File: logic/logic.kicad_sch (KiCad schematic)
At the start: 27 parts, among them J1 DIN41612_03x32_ABC, J2 Conn_02x05_Odd_Even, U1 TPIC6595, U2 TPIC6595, U3 TPIC6595, U4 TPIC6595, U5 TPIC6595, U6 TPIC6595, U7 TPIC6595, U8 TPIC6595, U9 74HC14

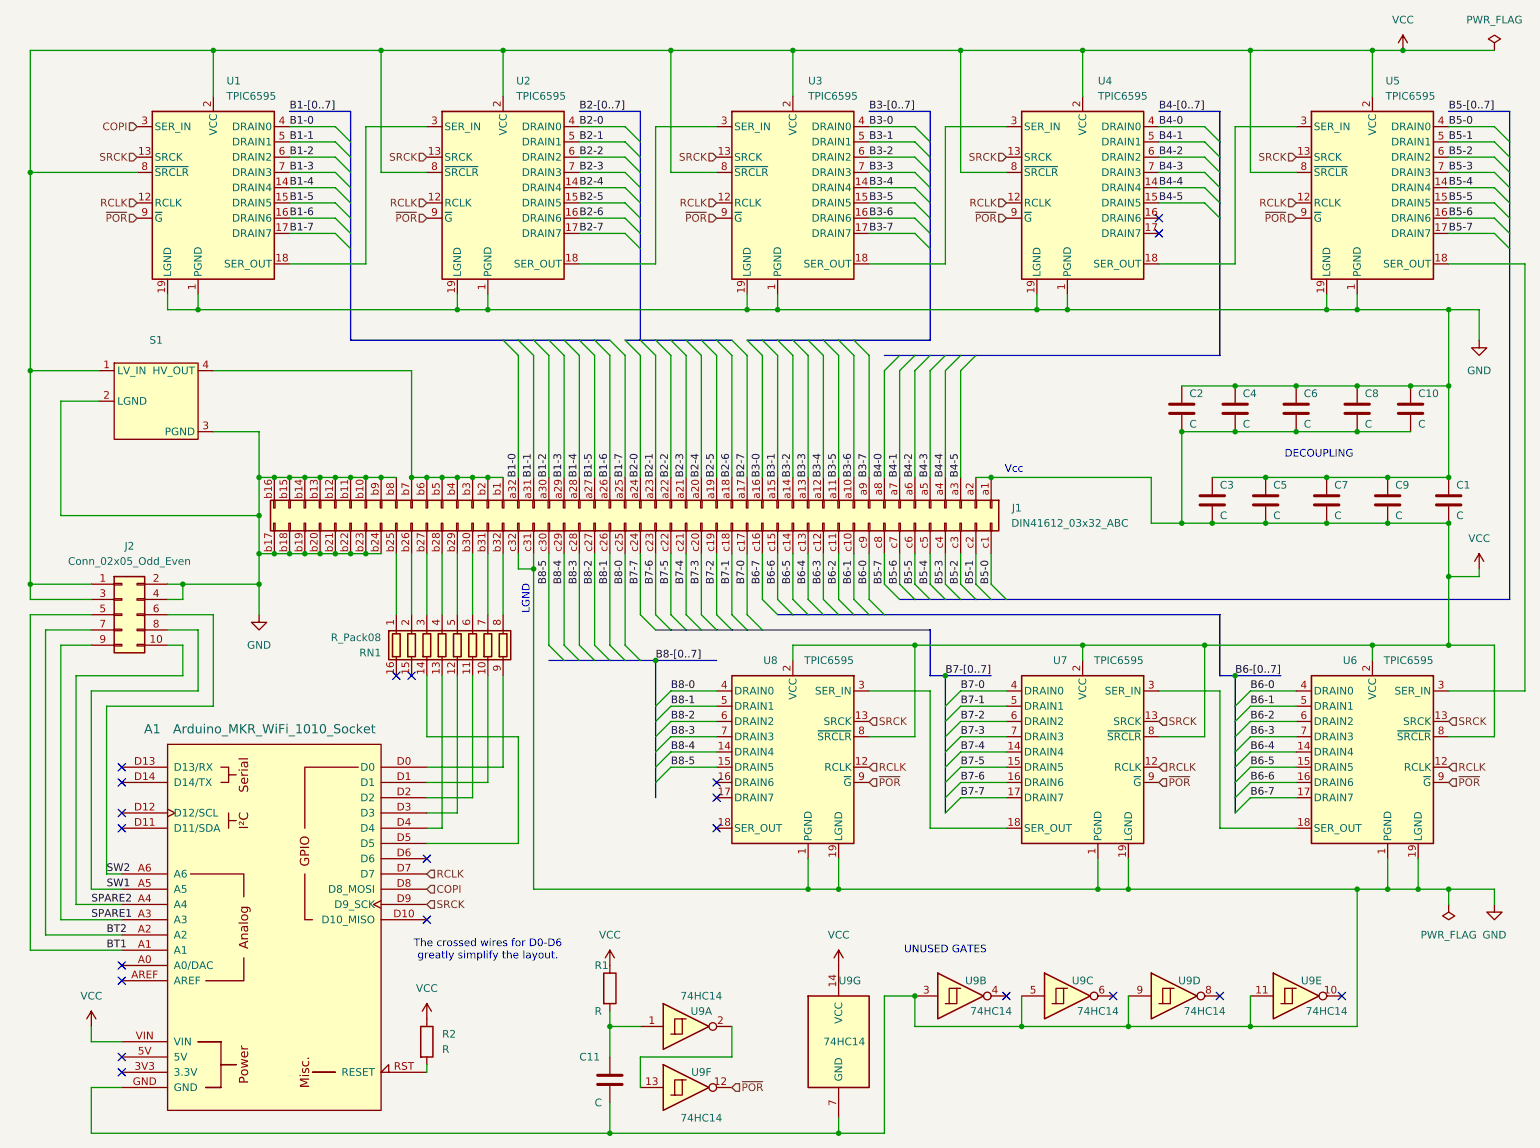
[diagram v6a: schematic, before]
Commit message: LEDs connected by 10-pin connector now. 96 pin connector simplified.
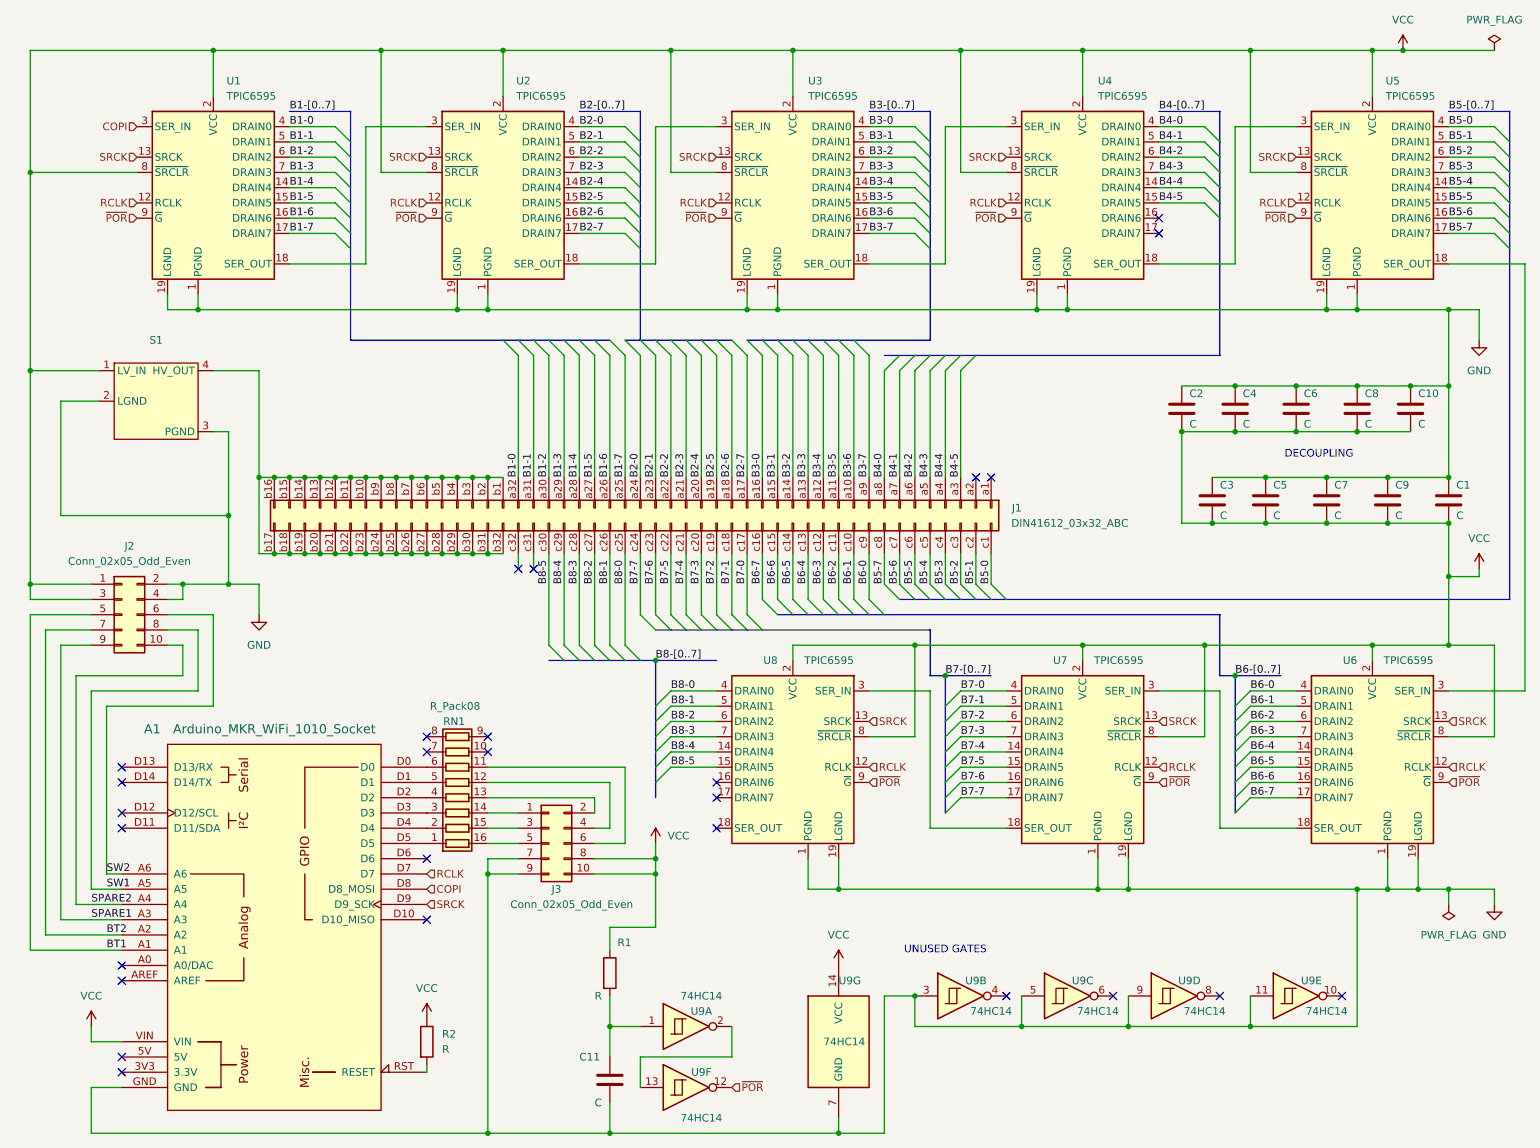
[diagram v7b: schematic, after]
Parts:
- added J3: Conn_02x05_Odd_Even, Connector_PinHeader_2.54mm:PinHeader_2x05_P2.54mm_Vertical, symbol Connector_Generic:Conn_02x05_Odd_Even
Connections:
- net GND: now also J3.7 (Pin_7), J3.9 (Pin_9); no longer J1.b10 (Pin_b10), J1.b11 (Pin_b11), J1.b12 (Pin_b12), J1.b13 (Pin_b13), J1.b14 (Pin_b14), J1.b15 (Pin_b15), J1.b16 (Pin_b16), J1.b17 (Pin_b17), J1.b18 (Pin_b18), J1.b19 (Pin_b19), J1.b20 (Pin_b20), J1.b21 (Pin_b21), J1.b22 (Pin_b22), J1.b23 (Pin_b23), J1.b24 (Pin_b24), J1.b8 (Pin_b8), J1.b9 (Pin_b9), J1.c31 (Pin_c31), J1.c32 (Pin_c32)
- net VCC: now also J3.10 (Pin_10), J3.8 (Pin_8); no longer J1.a1 (Pin_a1), J1.a2 (Pin_a2)
- net at A1.D0: now also RN1.6 (R6.1); no longer RN1.9 (R8.2)
- net at A1.D1: now also RN1.5 (R5.1); no longer RN1.10 (R7.2)
- net at RN1.11 (R6.2): now also J3.6 (Pin_6); no longer A1.D2
- net at RN1.12 (R5.2): now also J3.4 (Pin_4); no longer A1.D3
- net at RN1.13 (R4.2): now also J3.2 (Pin_2); no longer A1.D4
- net at RN1.14 (R3.2): now also J3.1 (Pin_1); no longer A1.D5
- net at RN1.1 (R1.1): now also A1.D5; no longer J1.b25 (Pin_b25)
- net at RN1.15 (R2.2): now also J3.3 (Pin_3)
- net at RN1.16 (R1.2): now also J3.5 (Pin_5)
- net at RN1.2 (R2.1): now also A1.D4; no longer J1.b26 (Pin_b26)
- net at RN1.3 (R3.1): now also A1.D3; no longer J1.b27 (Pin_b27)
- net at RN1.4 (R4.1): now also A1.D2; no longer J1.b28 (Pin_b28)
- net at J1.b29 (Pin_b29): now also J1.b1 (Pin_b1), J1.b10 (Pin_b10), J1.b11 (Pin_b11), J1.b12 (Pin_b12), J1.b13 (Pin_b13), J1.b14 (Pin_b14), J1.b15 (Pin_b15), J1.b16 (Pin_b16), J1.b17 (Pin_b17), J1.b18 (Pin_b18), J1.b19 (Pin_b19), J1.b2 (Pin_b2), J1.b20 (Pin_b20), J1.b21 (Pin_b21), J1.b22 (Pin_b22), J1.b23 (Pin_b23), J1.b24 (Pin_b24), J1.b25 (Pin_b25), J1.b26 (Pin_b26), J1.b27 (Pin_b27), J1.b28 (Pin_b28), J1.b3 (Pin_b3), J1.b30 (Pin_b30), J1.b31 (Pin_b31), J1.b32 (Pin_b32), J1.b4 (Pin_b4), J1.b5 (Pin_b5), J1.b6 (Pin_b6), J1.b7 (Pin_b7), J1.b8 (Pin_b8), J1.b9 (Pin_b9), S1.4 (HV_OUT); no longer RN1.5 (R5.1)
- net at RN1.7 (R7.1): no longer J1.b31 (Pin_b31)
- net at RN1.8 (R8.1): no longer J1.b32 (Pin_b32)
- no-connect marks 21 -> 27
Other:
- note removed: "LGND"
- note removed: "The crossed wires for D0-D6 greatly simplify the layout."
- note removed: "Vcc"
- moved on the sheet: RN1

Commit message: Add low voltage supply to logic board
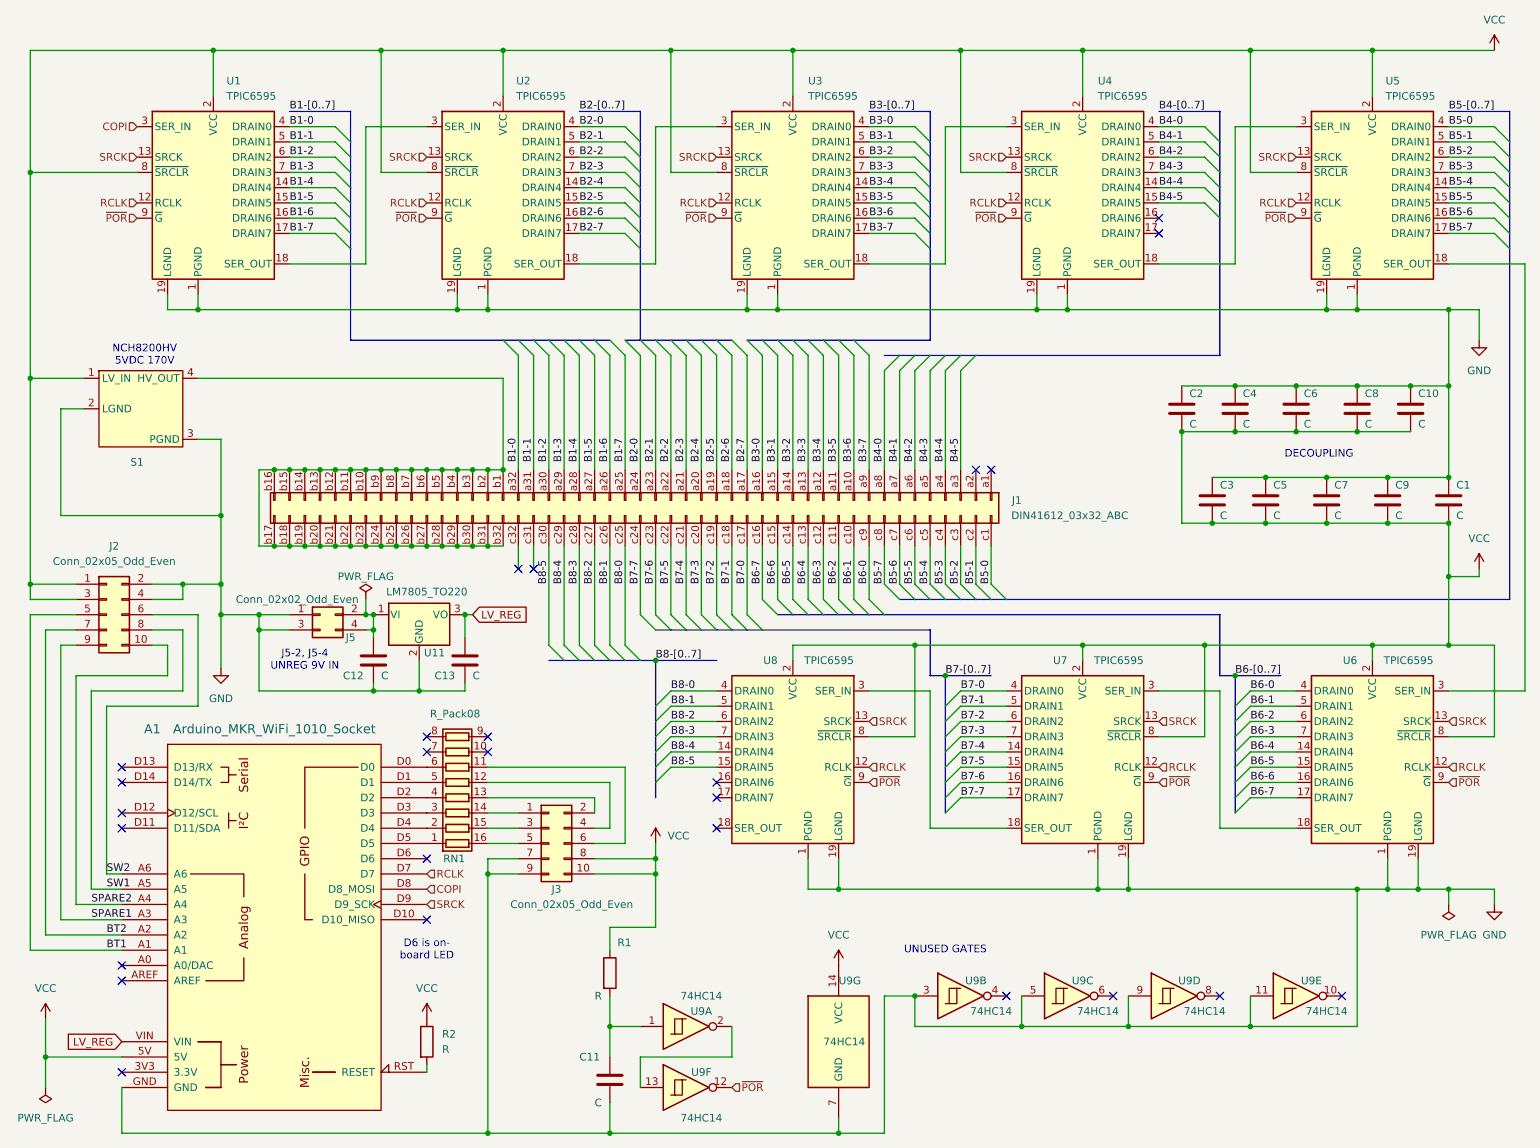
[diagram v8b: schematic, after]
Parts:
- added C12, C13: C, Capacitor_THT:C_Disc_D3.4mm_W2.1mm_P2.50mm, symbol Device:C
- added J5: Conn_02x02_Odd_Even, symbol Connector_Generic:Conn_02x02_Odd_Even
- added U11: LM7805_TO220, Package_TO_SOT_THT:TO-220-3_Vertical, symbol Regulator_Linear:LM7805_TO220
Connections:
- net GND: now also C12.2, C13.2, J5.1 (Pin_1), J5.3 (Pin_3), U11.2 (GND)
- net VCC: now also A1.5V; no longer A1.VIN
- new net: C12.1, J5.2 (Pin_2), J5.4 (Pin_4), U11.1 (VI)
- new net LV_REG: A1.VIN, C13.1, U11.3 (VO)
- no-connect marks 27 -> 26
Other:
- note added: "D6 is on- board LED"
- note added: "J5-2, J5-4 UNREG 9V IN"
- note added: "NCH8200HV 5VDC 170V"
- moved on the sheet: J1, J2, S1
